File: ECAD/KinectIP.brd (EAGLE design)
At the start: 64.8 x 60 mm, 12 parts, among them P5+ 2PIN-FEMALE-HEADER

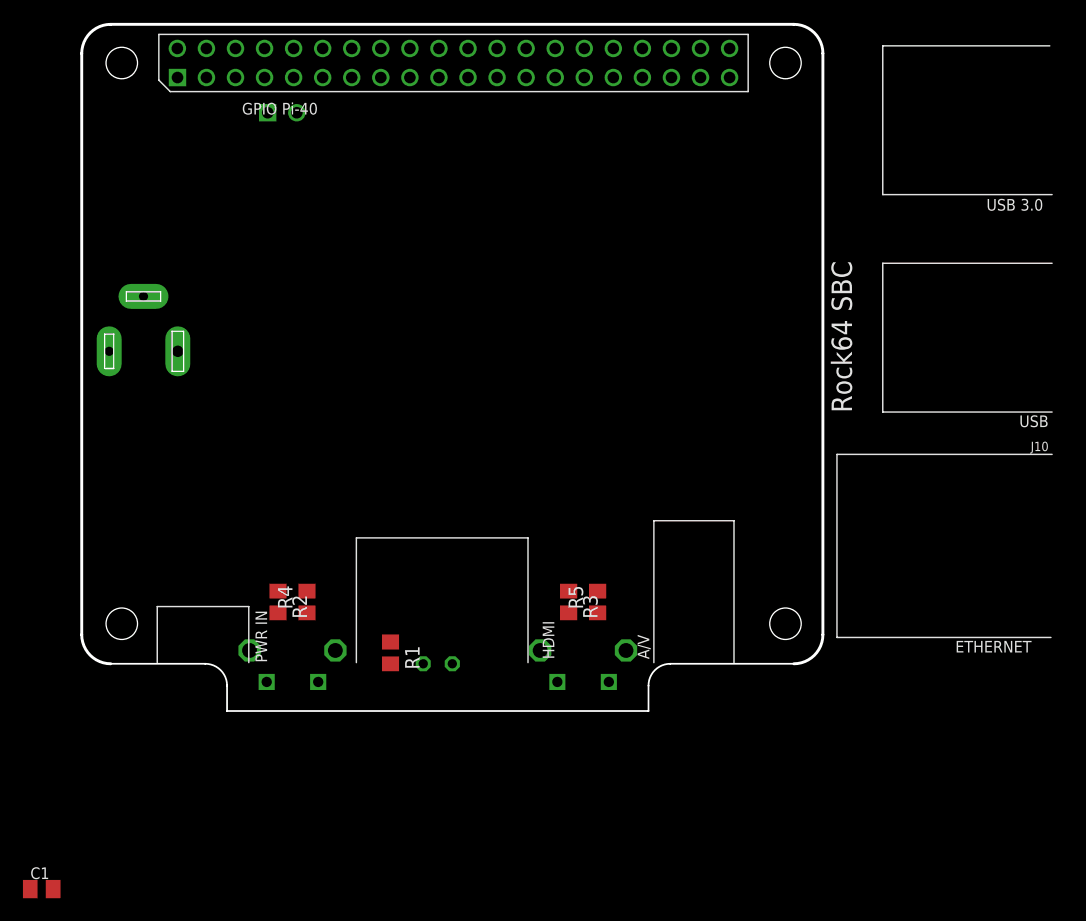
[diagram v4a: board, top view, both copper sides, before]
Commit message: add MP1584
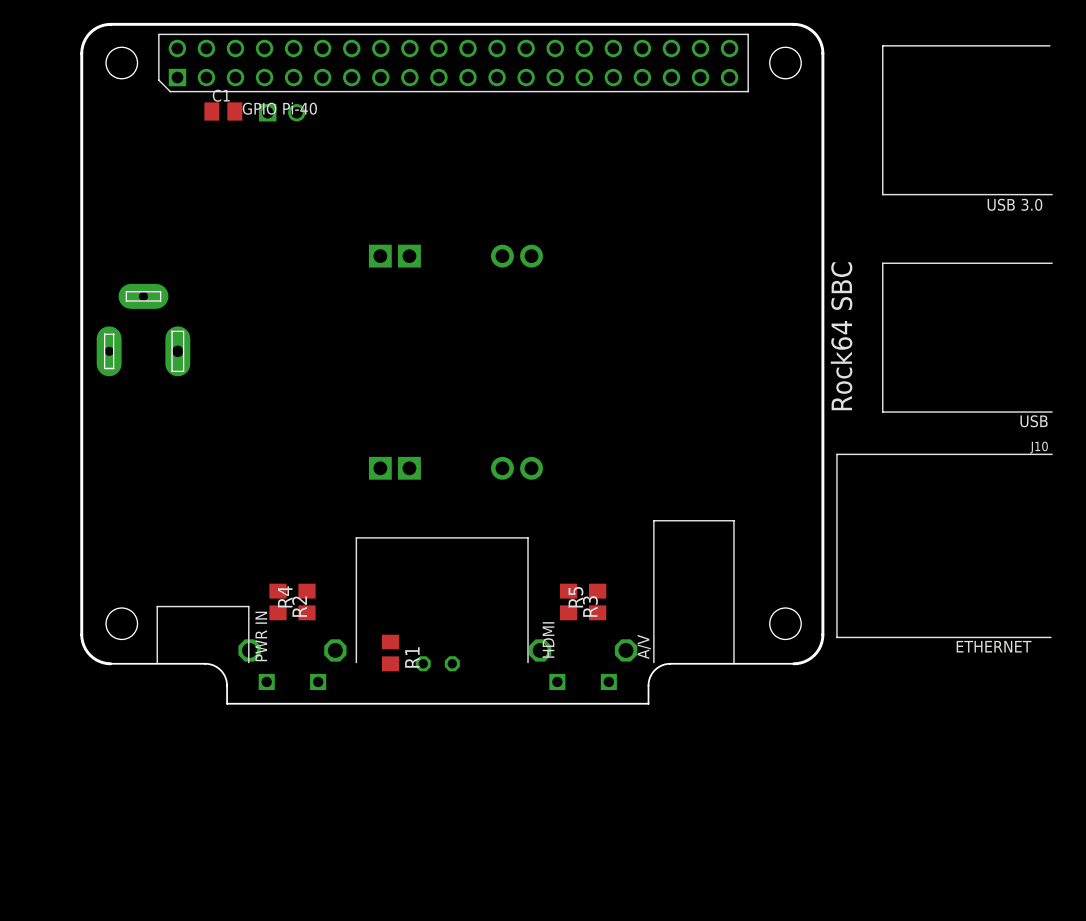
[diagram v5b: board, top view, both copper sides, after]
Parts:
- added 12V->5V: DC-DC-STEP-DOWN-MP1584, diy-modules:DC-DC-STEP-DOWN-MP1584
- C1: value (none) -> 100nF
- moved C1 69.8 mm to (12.4, 53.3)
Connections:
- new net +5V: 12V->5V.OUT+.1, 12V->5V.OUT+.2, C1.1, PCB2.P$2, PCB2.P$4
- net +12V: now also 12V->5V.IN+.1, 12V->5V.IN+.2
- net 0V: now also 12V->5V.IN-.1, 12V->5V.IN-.2, 12V->5V.OUT-.1, 12V->5V.OUT-.2, C1.2
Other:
- board size 64.8 x 60 mm -> 64.8 x 59.4 mm
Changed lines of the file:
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@@
 </layers>
 <board>
-<fusionsync huburn="a.cGVyc29uYWw6dWUyOGRkYTQ5" projecturn="a.cGVyc29uYWw6dWUyOGRkYTQ5IzIwMTkwNzIxMjA0NzU1MDc2" f3durn="urn:adsk.wipprod:dm.lineage:51sdf3HBRlSp9b0qTDdM7A" pcbguid="17f93904-f036-442f-8767-7531df551236" lastpulledtime="2019-07-25T10:40:12Z" lastsyncedchangeguid="30b88b88-6244-209e-32c0-b88ed1906c49"/>
+<fusionsync huburn="a.cGVyc29uYWw6dWUyOGRkYTQ5" projecturn="a.cGVyc29uYWw6dWUyOGRkYTQ5IzIwMTkwNzIxMjA0NzU1MDc2" f3durn="urn:adsk.wipprod:dm.lineage:51sdf3HBRlSp9b0qTDdM7A" pcbguid="17f93904-f036-442f-8767-7531df551236" lastpulledtime="2019-07-25T10:40:12Z" lastsyncedchangeguid="951c594f-2a3f-7381-0e4c-9582c71d1740"/>
 <plain>
 <wire x1="2.54" y1="60.96" x2="0" y2="58.42" width="0.254" layer="20" curve="90"/>
@@
 <wire x1="2.54" y1="5.08" x2="10.795" y2="5.08" width="0.1524" layer="20"/>
 <wire x1="10.795" y1="5.08" x2="12.7" y2="3.175" width="0.1524" layer="20" curve="-90"/>
-<wire x1="12.7" y1="3.175" x2="12.7" y2="0.9525" width="0.1524" layer="20"/>
-<wire x1="12.7" y1="0.9525" x2="49.53" y2="0.9525" width="0.1524" layer="20"/>
-<wire x1="49.53" y1="0.9525" x2="49.53" y2="3.175" width="0.1524" layer="20"/>
+<wire x1="12.7" y1="3.175" x2="12.7" y2="1.5875" width="0.1524" layer="20"/>
+<wire x1="12.7" y1="1.5875" x2="49.53" y2="1.5875" width="0.1524" layer="20"/>
+<wire x1="49.53" y1="1.5875" x2="49.53" y2="3.175" width="0.1524" layer="20"/>
 <wire x1="49.53" y1="3.175" x2="51.435" y2="5.08" width="0.1524" layer="20" curve="-90"/>
 <wire x1="51.435" y1="5.08" x2="62.23" y2="5.08" width="0.1524" layer="20"/>
@@
 <attribute name="VALUE" x="27.559" y="1.905" size="1.27" layer="28" ratio="10" rot="MR90"/>
 </element>
-<element name="C1" library="rcl" library_urn="urn:adsk.eagle:library:334" package="C0805K" package3d_urn="urn:adsk.eagle:package:23681/2" value="" x="-3.4925" y="-14.605" smashed="yes">
-<attribute name="NAME" x="-4.4925" y="-13.73" size="1.016" layer="25"/>
-<attribute name="POPULARITY" value="52" x="-3.4925" y="-14.605" size="1.778" layer="27" display="off"/>
-<attribute name="SPICEPREFIX" value="C" x="-3.4925" y="-14.605" size="1.778" layer="27" display="off"/>
-<attribute name="VALUE" x="-4.4925" y="-16.505" size="1.016" layer="27"/>
+<element name="C1" library="rcl" library_urn="urn:adsk.eagle:library:334" package="C0805K" package3d_urn="urn:adsk.eagle:package:23681/2" value="100nF" x="12.3825" y="53.34" smashed="yes">
+<attribute name="NAME" x="11.3825" y="54.215" size="1.016" layer="25"/>
+<attribute name="POPULARITY" value="52" x="12.3825" y="53.34" size="1.778" layer="27" display="off"/>
+<attribute name="SPICEPREFIX" value="C" x="12.3825" y="53.34" size="1.778" layer="27" display="off"/>
+<attribute name="VALUE" x="11.3825" y="51.44" size="1.016" layer="27"/>
+</element>
+<element name="12V-&gt;5V" library="diy-modules" library_urn="urn:adsk.eagle:library:12361804" package="DC-DC-STEP-DOWN-MP1584" package3d_urn="urn:adsk.eagle:package:12362133/2" value="DC-DC-STEP-DOWN-MP1584" x="32.7025" y="31.4325" smashed="yes" rot="MR90">
+<attribute name="NAME" x="42.2275" y="31.4325" size="1.27" layer="26" rot="MR90" align="bottom-center"/>
+<attribute name="VALUE" x="23.1775" y="31.4325" size="1.27" layer="28" rot="MR90" align="top-center"/>
 </element>
 </elements>
@@
 <contactref element="J1" pad="1"/>
 <contactref element="J1" pad="2"/>
-<wire x1="42.545" y1="11.4275" x2="38.8366" y2="56.3118" width="0" layer="19" extent="1-1"/>
-<wire x1="40.065" y1="6.2425" x2="42.545" y2="11.4275" width="0" layer="19" extent="1-1"/>
-<wire x1="26.9875" y1="6.9825" x2="40.065" y2="6.2425" width="0" layer="19" extent="1-1"/>
+<contactref element="12V-&gt;5V" pad="IN-.1"/>
+<contactref element="12V-&gt;5V" pad="IN-.2"/>
+<contactref element="12V-&gt;5V" pad="OUT-.1"/>
+<contactref element="12V-&gt;5V" pad="OUT-.2"/>
+<contactref element="C1" pad="2"/>
+<wire x1="13.3825" y1="53.34" x2="38.8366" y2="56.3118" width="0" layer="19" extent="1-1"/>
+<wire x1="5.3975" y1="37.185" x2="13.3825" y2="53.34" width="0" layer="19" extent="1-1"/>
+<wire x1="2.3975" y1="32.385" x2="5.3975" y2="37.185" width="0" layer="19" extent="1-1"/>
+<wire x1="17.145" y1="11.4275" x2="13.3825" y2="53.34" width="0" layer="19" extent="1-1"/>
+<wire x1="14.665" y1="6.2425" x2="17.145" y2="11.4275" width="0" layer="19" extent="1-1"/>
+<wire x1="22.165" y1="6.2425" x2="17.145" y2="11.4275" width="0" layer="19" extent="1-1"/>
+<wire x1="26.9875" y1="6.9825" x2="22.165" y2="6.2425" width="0" layer="19" extent="1-1"/>
+<wire x1="40.065" y1="6.2425" x2="26.9875" y2="6.9825" width="0" layer="19" extent="1-1"/>
+<wire x1="42.545" y1="11.4275" x2="40.065" y2="6.2425" width="0" layer="19" extent="1-1"/>
 <wire x1="47.565" y1="6.2425" x2="42.545" y2="11.4275" width="0" layer="19" extent="1-1"/>
-<wire x1="22.165" y1="6.2425" x2="26.9875" y2="6.9825" width="0" layer="19" extent="1-1"/>
-<wire x1="17.145" y1="11.4275" x2="22.165" y2="6.2425" width="0" layer="19" extent="1-1"/>
-<wire x1="14.665" y1="6.2425" x2="17.145" y2="11.4275" width="0" layer="19" extent="1-1"/>
-<wire x1="2.3975" y1="32.385" x2="14.665" y2="6.2425" width="0" layer="19" extent="1-1"/>
-<wire x1="5.3975" y1="37.185" x2="2.3975" y2="32.385" width="0" layer="19" extent="1-1"/>
+<wire x1="39.3065" y1="40.7035" x2="14.665" y2="6.2425" width="0" layer="19" extent="1-1"/>
+<wire x1="36.7665" y1="40.7035" x2="39.3065" y2="40.7035" width="0" layer="19" extent="1-1"/>
+<wire x1="36.7665" y1="22.1615" x2="36.7665" y2="40.7035" width="0" layer="19" extent="1-1"/>
+<wire x1="39.3065" y1="22.1615" x2="36.7665" y2="22.1615" width="0" layer="19" extent="1-1"/>
 </signal>
 <signal name="N$1">
@@
 <signal name="+12V">
 <contactref element="J1" pad="3"/>
+<contactref element="12V-&gt;5V" pad="IN+.1"/>
+<contactref element="12V-&gt;5V" pad="IN+.2"/>
+<wire x1="28.6385" y1="22.1615" x2="8.3975" y2="32.385" width="0" layer="19" extent="1-1"/>
+<wire x1="26.0985" y1="22.1615" x2="28.6385" y2="22.1615" width="0" layer="19" extent="1-1"/>
+</signal>
+<signal name="+5V">
+<contactref element="12V-&gt;5V" pad="OUT+.1"/>
+<contactref element="12V-&gt;5V" pad="OUT+.2"/>
+<contactref element="C1" pad="1"/>
+<contactref element="PCB2" pad="P$4"/>
+<contactref element="PCB2" pad="P$2"/>
+<wire x1="8.3566" y1="58.8518" x2="10.8966" y2="58.8518" width="0" layer="19" extent="1-1"/>
+<wire x1="11.3825" y1="53.34" x2="10.8966" y2="58.8518" width="0" layer="19" extent="1-1"/>
+<wire x1="26.0985" y1="40.7035" x2="11.3825" y2="53.34" width="0" layer="19" extent="1-1"/>
+<wire x1="28.6385" y1="40.7035" x2="26.0985" y2="40.7035" width="0" layer="19" extent="1-1"/>
 </signal>
 </signals>
